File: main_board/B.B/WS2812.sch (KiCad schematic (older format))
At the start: 120 parts

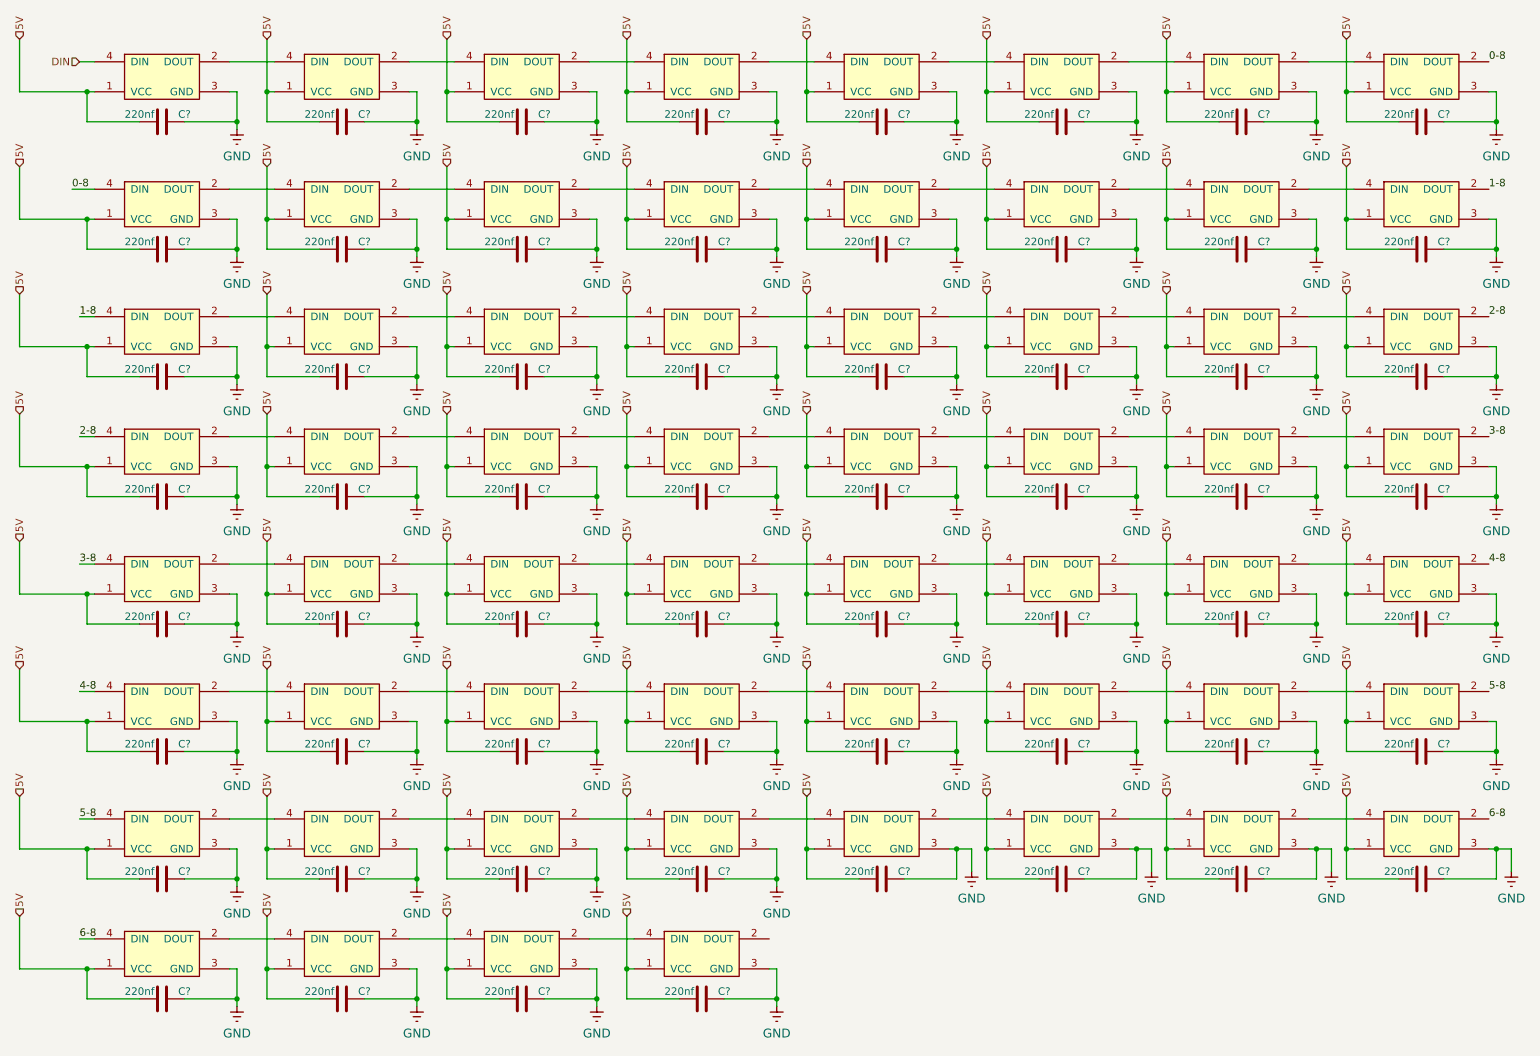
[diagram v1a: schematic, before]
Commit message: complete_preparation_to_drawing_PCB
footprint for all component and LCSC code for everything for mounting in JLCPCB
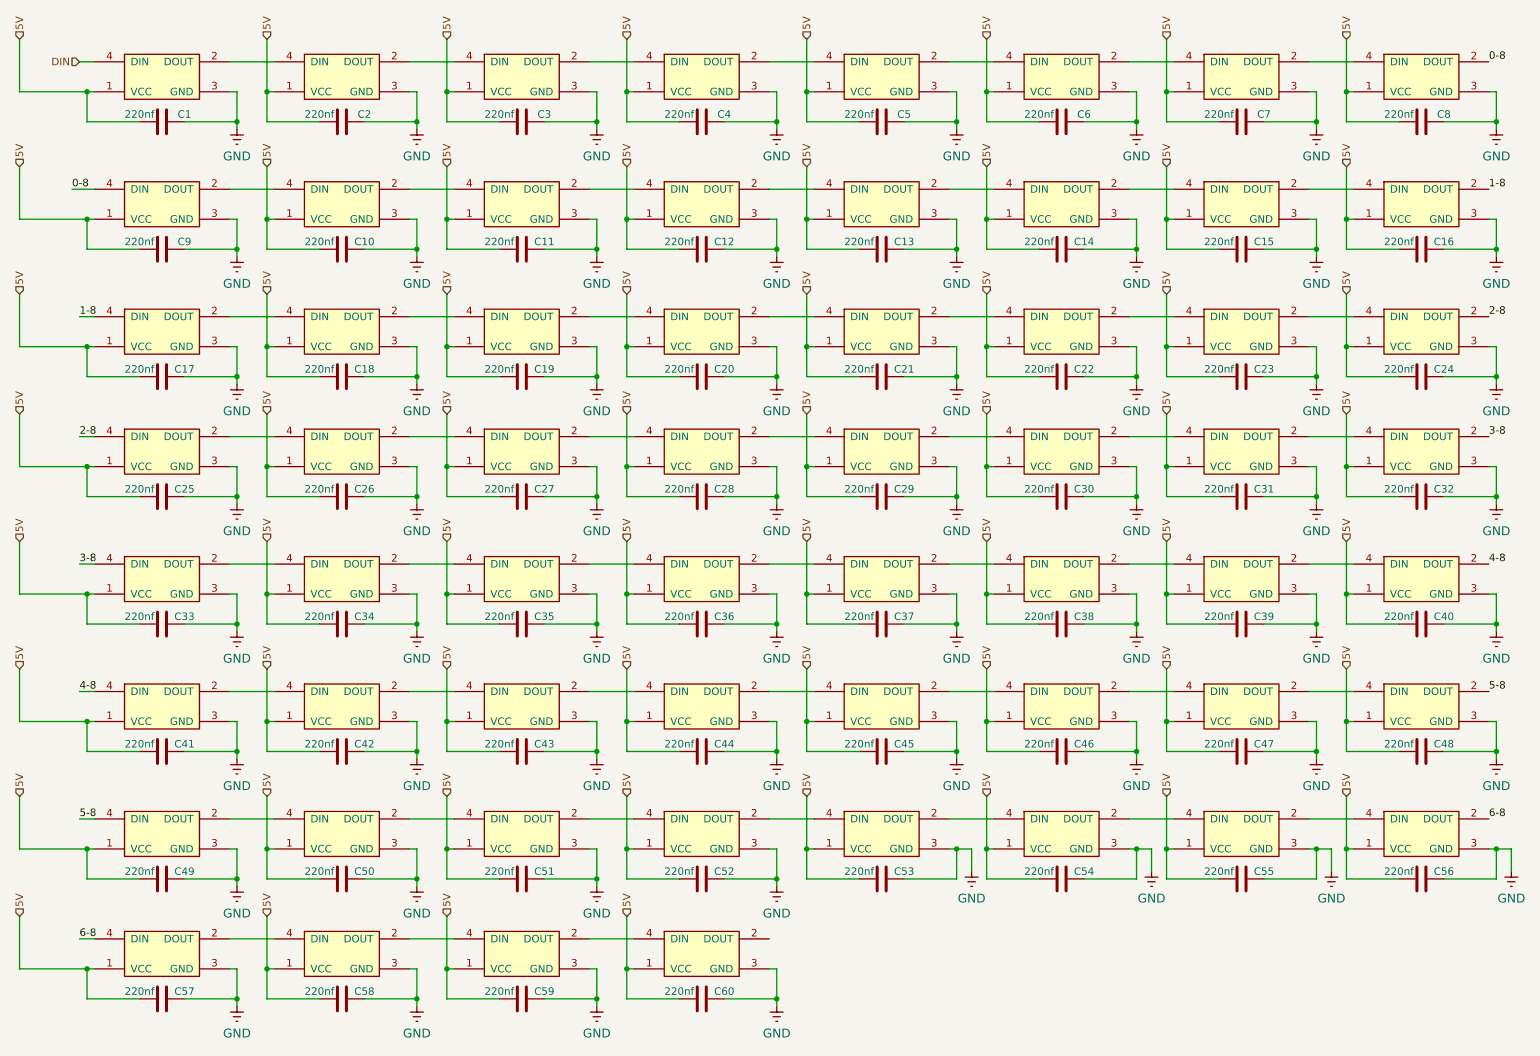
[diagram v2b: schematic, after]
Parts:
- removed U? (x59): WS2812, symbol B.B-eagle-import:WS2812
- added U10, U11, U12, U13, U14, U15, U16, U17, U18, U19, U2, U20, U21, U22, U23, U24, U25, U26, U27, U28, U29, U3, U30, U31, U32, U33, U34, U35, U36, U37, U38, U39, U4, U40, U41, U42, U43, U44, U45, U46, U47, U48, U49, U5, U50, U51, U52, U53, U54, U55, U56, U57, U58, U59, U6, U7, U74, U8, U9: WS2812, BB:WS2812, symbol B.B-eagle-import:WS2812
- U1: renamed from ?; footprint (none) -> BB:WS2812
- gave numbers to parts that had none: 60
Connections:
- net 0-8: now also U8.2 (DOUT), U9.4 (DIN)
- net 1-8: now also U16.2 (DOUT), U17.4 (DIN)
- net 2-8: now also U24.2 (DOUT), U25.4 (DIN)
- net 3-8: now also U32.2 (DOUT), U33.4 (DIN)
- net 4-8: now also U40.2 (DOUT), U41.4 (DIN)
- net 5-8: now also U48.2 (DOUT), U49.4 (DIN)
- net 5V: now also U10.1 (VCC), U11.1 (VCC), U12.1 (VCC), U13.1 (VCC), U14.1 (VCC), U15.1 (VCC), U16.1 (VCC), U17.1 (VCC), U18.1 (VCC), U19.1 (VCC), U2.1 (VCC), U20.1 (VCC), U21.1 (VCC), U22.1 (VCC), U23.1 (VCC), U24.1 (VCC), U25.1 (VCC), U26.1 (VCC), U27.1 (VCC), U28.1 (VCC), U29.1 (VCC), U3.1 (VCC), U30.1 (VCC), U31.1 (VCC), U32.1 (VCC), U33.1 (VCC), U34.1 (VCC), U35.1 (VCC), U36.1 (VCC), U37.1 (VCC), U38.1 (VCC), U39.1 (VCC), U4.1 (VCC), U40.1 (VCC), U41.1 (VCC), U42.1 (VCC), U43.1 (VCC), U44.1 (VCC), U45.1 (VCC), U46.1 (VCC), U47.1 (VCC), U48.1 (VCC), U49.1 (VCC), U5.1 (VCC), U50.1 (VCC), U51.1 (VCC), U52.1 (VCC), U53.1 (VCC), U54.1 (VCC), U55.1 (VCC), U56.1 (VCC), U57.1 (VCC), U58.1 (VCC), U59.1 (VCC), U6.1 (VCC), U7.1 (VCC), U74.1 (VCC), U8.1 (VCC), U9.1 (VCC)
- net 6-8: now also U56.2 (DOUT), U57.4 (DIN)
- net at U1.2 (DOUT): now also U2.4 (DIN)
- net at C2.1: now also U2.3 (GND)
- net at C3.1: now also U3.3 (GND)
- net at C4.1: now also U4.3 (GND)
- net at C5.1: now also U5.3 (GND)
- net at C6.1: now also U6.3 (GND)
- net at C7.1: now also U7.3 (GND)
- net at C8.1: now also U8.3 (GND)
- net at C9.1: now also U9.3 (GND)
- net at C10.1: now also U10.3 (GND)
- net at C11.1: now also U11.3 (GND)
- net at C12.1: now also U12.3 (GND)
- net at C13.1: now also U13.3 (GND)
- net at C14.1: now also U14.3 (GND)
- net at C15.1: now also U15.3 (GND)
- net at C16.1: now also U16.3 (GND)
- net at C17.1: now also U17.3 (GND)
- net at C18.1: now also U18.3 (GND)
- net at C19.1: now also U19.3 (GND)
- net at C20.1: now also U20.3 (GND)
- net at C21.1: now also U21.3 (GND)
- net at C22.1: now also U22.3 (GND)
- net at C23.1: now also U23.3 (GND)
- net at C24.1: now also U24.3 (GND)
- net at C25.1: now also U25.3 (GND)
- net at C26.1: now also U26.3 (GND)
- net at C27.1: now also U27.3 (GND)
- net at C28.1: now also U28.3 (GND)
- net at C29.1: now also U29.3 (GND)
- net at C30.1: now also U30.3 (GND)
- net at C31.1: now also U31.3 (GND)
- net at C32.1: now also U32.3 (GND)
- net at C33.1: now also U33.3 (GND)
- net at C34.1: now also U34.3 (GND)
- net at C35.1: now also U35.3 (GND)
- net at C36.1: now also U36.3 (GND)
- net at C37.1: now also U37.3 (GND)
- net at C38.1: now also U38.3 (GND)
- net at C39.1: now also U39.3 (GND)
- net at C40.1: now also U40.3 (GND)
- net at C48.1: now also U48.3 (GND)
- net at C47.1: now also U47.3 (GND)
- net at C46.1: now also U46.3 (GND)
- net at C45.1: now also U45.3 (GND)
- net at C44.1: now also U44.3 (GND)
- net at C43.1: now also U43.3 (GND)
- net at C42.1: now also U42.3 (GND)
- net at C41.1: now also U41.3 (GND)
- net at C49.1: now also U49.3 (GND)
- net at C50.1: now also U50.3 (GND)
- net at C51.1: now also U51.3 (GND)
- net at C52.1: now also U52.3 (GND)
- net at C53.1: now also U53.3 (GND)
- net at C54.1: now also U54.3 (GND)
- net at C55.1: now also U55.3 (GND)
- net at C56.1: now also U56.3 (GND)
- net at C57.1: now also U57.3 (GND)
- net at C58.1: now also U58.3 (GND)
- net at C59.1: now also U59.3 (GND)
- net at C60.1: now also U74.3 (GND)
- new net: U2.2 (DOUT), U3.4 (DIN)
- new net: U3.2 (DOUT), U4.4 (DIN)
- new net: U4.2 (DOUT), U5.4 (DIN)
- new net: U5.2 (DOUT), U6.4 (DIN)
- new net: U6.2 (DOUT), U7.4 (DIN)
- new net: U7.2 (DOUT), U8.4 (DIN)
- new net: U10.4 (DIN), U9.2 (DOUT)
- new net: U10.2 (DOUT), U11.4 (DIN)
- new net: U11.2 (DOUT), U12.4 (DIN)
- new net: U12.2 (DOUT), U13.4 (DIN)
- new net: U13.2 (DOUT), U14.4 (DIN)
- new net: U14.2 (DOUT), U15.4 (DIN)
- new net: U15.2 (DOUT), U16.4 (DIN)
- new net: U17.2 (DOUT), U18.4 (DIN)
- new net: U18.2 (DOUT), U19.4 (DIN)
- new net: U19.2 (DOUT), U20.4 (DIN)
- new net: U20.2 (DOUT), U21.4 (DIN)
- new net: U21.2 (DOUT), U22.4 (DIN)
- new net: U22.2 (DOUT), U23.4 (DIN)
- new net: U23.2 (DOUT), U24.4 (DIN)
- new net: U25.2 (DOUT), U26.4 (DIN)
- new net: U26.2 (DOUT), U27.4 (DIN)
- new net: U27.2 (DOUT), U28.4 (DIN)
- new net: U28.2 (DOUT), U29.4 (DIN)
- new net: U29.2 (DOUT), U30.4 (DIN)
- new net: U30.2 (DOUT), U31.4 (DIN)
- new net: U31.2 (DOUT), U32.4 (DIN)
- new net: U33.2 (DOUT), U34.4 (DIN)
- new net: U34.2 (DOUT), U35.4 (DIN)
- new net: U35.2 (DOUT), U36.4 (DIN)
- new net: U36.2 (DOUT), U37.4 (DIN)
- new net: U37.2 (DOUT), U38.4 (DIN)
- new net: U38.2 (DOUT), U39.4 (DIN)
- new net: U39.2 (DOUT), U40.4 (DIN)
- new net: U41.2 (DOUT), U42.4 (DIN)
- new net: U42.2 (DOUT), U43.4 (DIN)
- new net: U43.2 (DOUT), U44.4 (DIN)
- new net: U44.2 (DOUT), U45.4 (DIN)
- new net: U45.2 (DOUT), U46.4 (DIN)
- new net: U46.2 (DOUT), U47.4 (DIN)
- new net: U47.2 (DOUT), U48.4 (DIN)
- new net: U49.2 (DOUT), U50.4 (DIN)
- new net: U50.2 (DOUT), U51.4 (DIN)
- new net: U51.2 (DOUT), U52.4 (DIN)
- new net: U52.2 (DOUT), U53.4 (DIN)
- new net: U53.2 (DOUT), U54.4 (DIN)
- new net: U54.2 (DOUT), U55.4 (DIN)
- new net: U55.2 (DOUT), U56.4 (DIN)
- new net: U57.2 (DOUT), U58.4 (DIN)
- new net: U58.2 (DOUT), U59.4 (DIN)
- new net: U59.2 (DOUT), U74.4 (DIN)

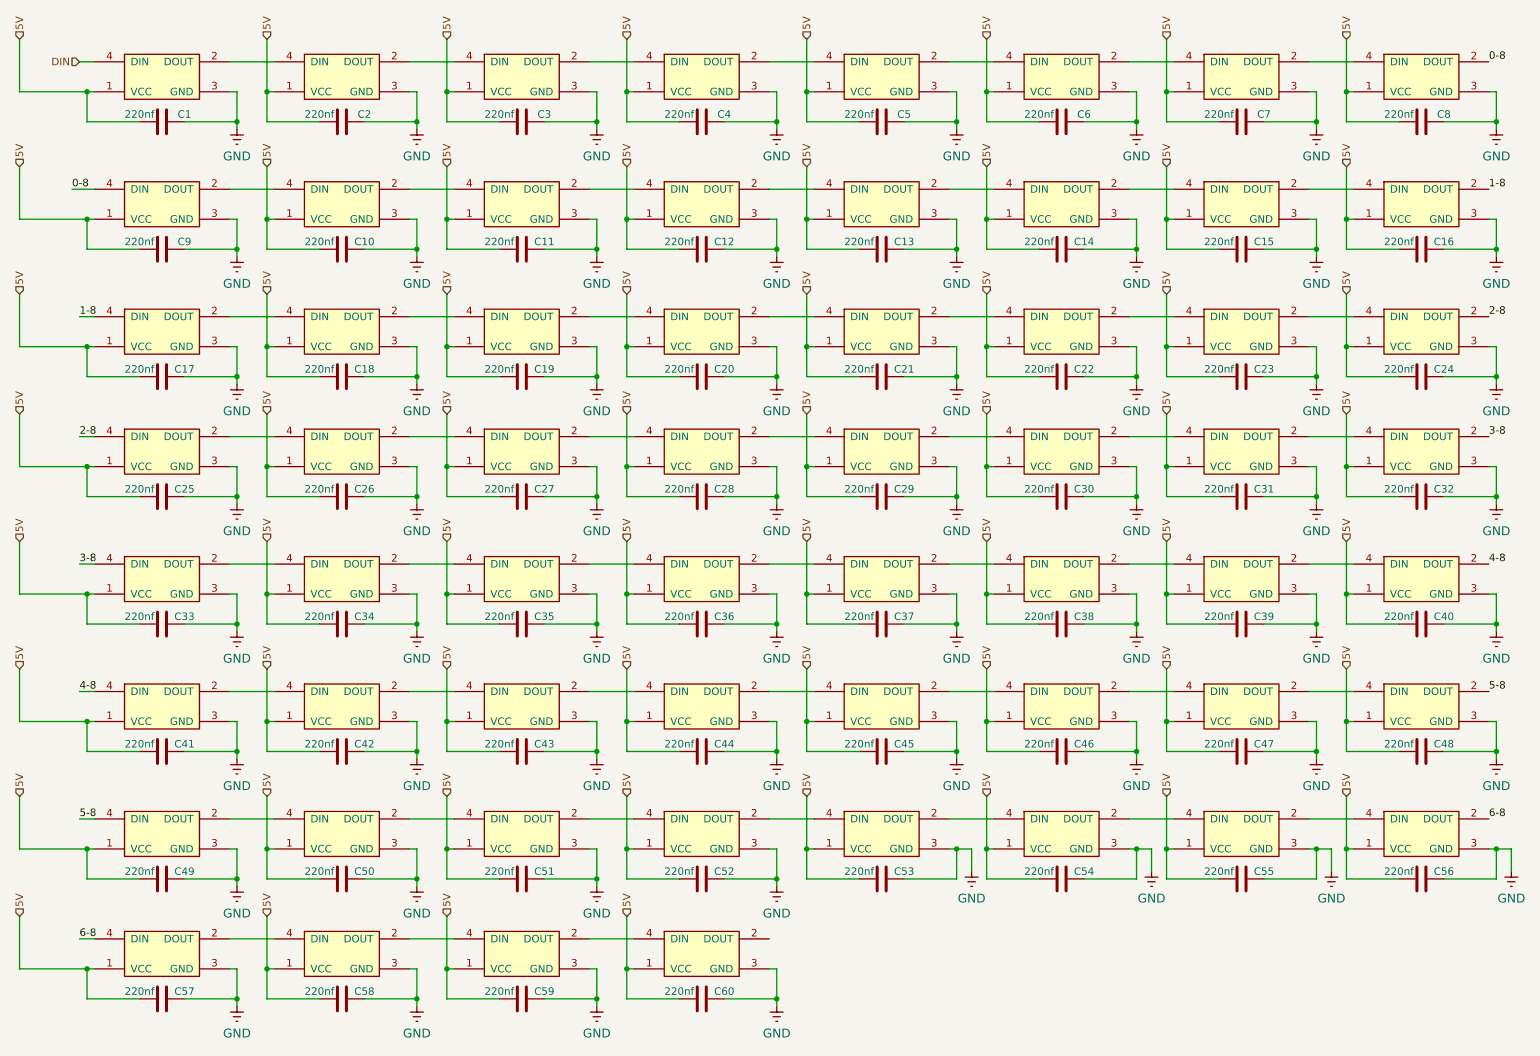
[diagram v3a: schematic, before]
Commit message: orezavani
smazaní A9G, SD karty, a zvuku
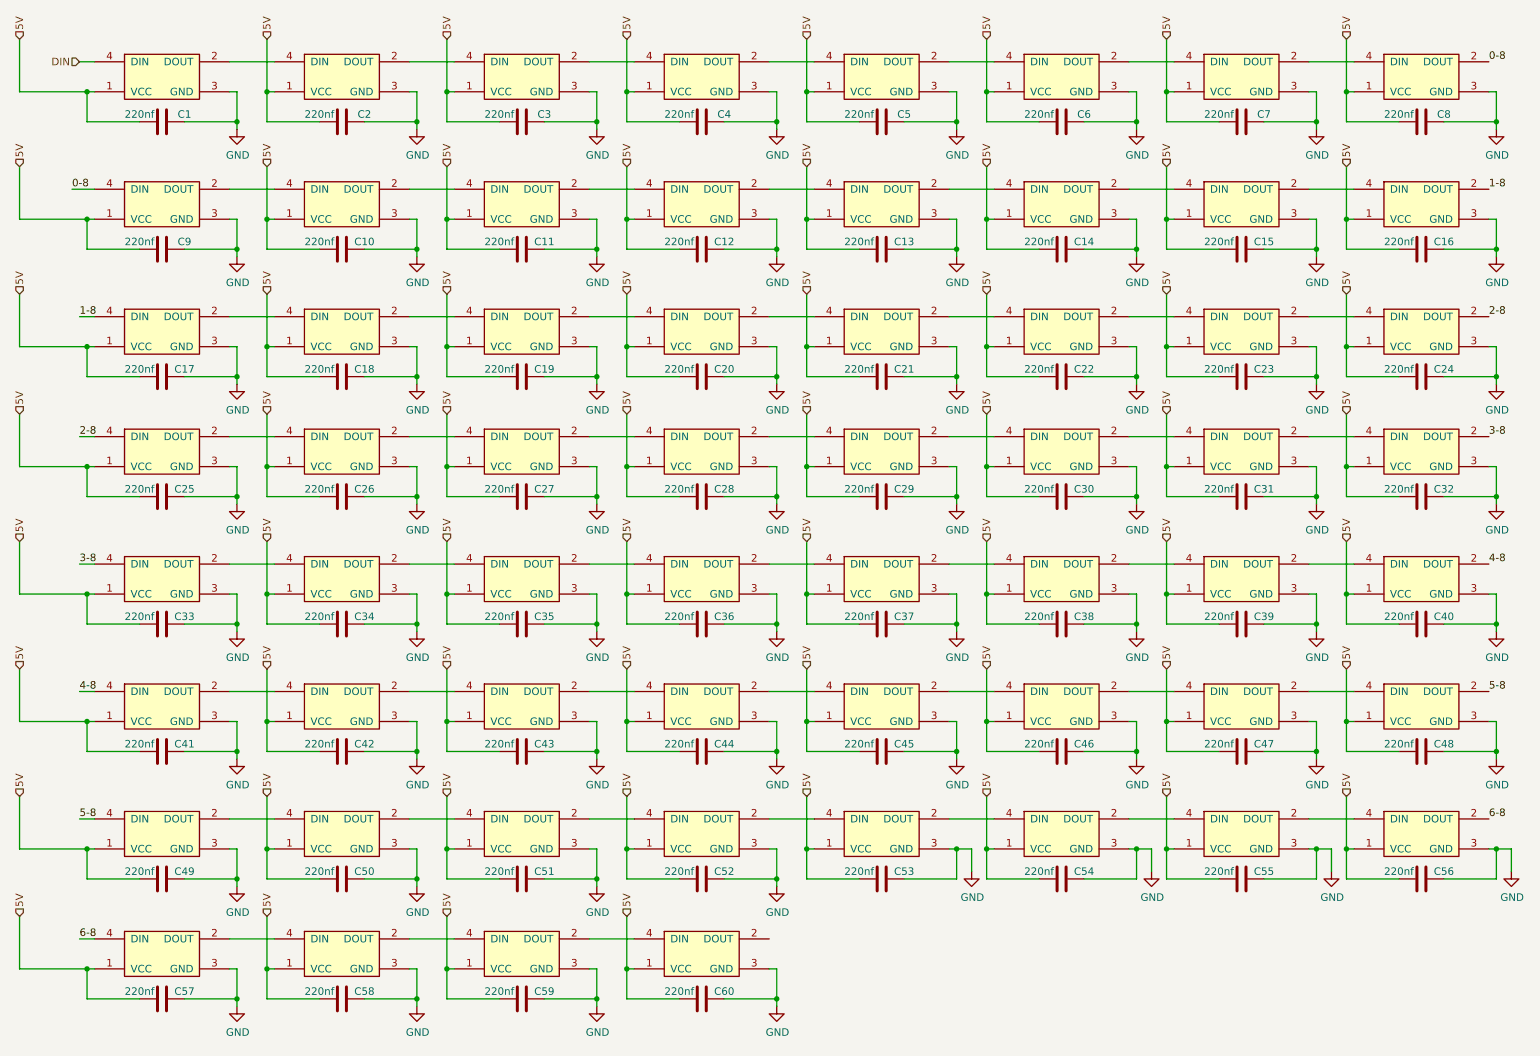
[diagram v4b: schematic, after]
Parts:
- removed U1, U10, U11, U12, U13, U14, U15, U16, U17, U18, U19, U2, U20, U21, U22, U23, U24, U25, U26, U27, U28, U29, U3, U30, U31, U32, U33, U34, U35, U36, U37, U38, U39, U4, U40, U41, U42, U43, U44, U45, U46, U47, U48, U49, U5, U50, U51, U52, U53, U54, U55, U56, U57, U58, U59, U6, U7, U74, U8, U9: WS2812, BB:WS2812, symbol B.B-eagle-import:WS2812
- added U? (x60): WS2812, BB:WS2812, symbol B.B-eagle-import:WS2812
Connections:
- net 0-8: now also U?.2 (DOUT), U?.4 (DIN)
- net 1-8: now also U?.2 (DOUT), U?.4 (DIN)
- net 2-8: now also U?.2 (DOUT), U?.4 (DIN)
- net 3-8: now also U?.2 (DOUT), U?.4 (DIN)
- net 4-8: now also U?.2 (DOUT), U?.4 (DIN)
- net 5-8: now also U?.2 (DOUT), U?.4 (DIN)
- net 5V: now also U?.1 (VCC), U?.1 (VCC), U?.1 (VCC), U?.1 (VCC), U?.1 (VCC), U?.1 (VCC), U?.1 (VCC), U?.1 (VCC), U?.1 (VCC), U?.1 (VCC), U?.1 (VCC), U?.1 (VCC), U?.1 (VCC), U?.1 (VCC), U?.1 (VCC), U?.1 (VCC), U?.1 (VCC), U?.1 (VCC), U?.1 (VCC), U?.1 (VCC), U?.1 (VCC), U?.1 (VCC), U?.1 (VCC), U?.1 (VCC), U?.1 (VCC), U?.1 (VCC), U?.1 (VCC), U?.1 (VCC), U?.1 (VCC), U?.1 (VCC), U?.1 (VCC), U?.1 (VCC), U?.1 (VCC), U?.1 (VCC), U?.1 (VCC), U?.1 (VCC), U?.1 (VCC), U?.1 (VCC), U?.1 (VCC), U?.1 (VCC), U?.1 (VCC), U?.1 (VCC), U?.1 (VCC), U?.1 (VCC), U?.1 (VCC), U?.1 (VCC), U?.1 (VCC), U?.1 (VCC), U?.1 (VCC), U?.1 (VCC), U?.1 (VCC), U?.1 (VCC), U?.1 (VCC), U?.1 (VCC), U?.1 (VCC), U?.1 (VCC), U?.1 (VCC), U?.1 (VCC), U?.1 (VCC), U?.1 (VCC)
- net 6-8: now also U?.2 (DOUT), U?.4 (DIN)
- net DIN: now also U?.4 (DIN)
- net GND: now reaches C1.1
- net GND: now also C10.1, C11.1, C12.1, C13.1, C14.1, C15.1, C16.1, C17.1, C18.1, C19.1, C2.1, C20.1, C21.1, C22.1, C23.1, C24.1, C25.1, C26.1, C27.1, C28.1, C29.1, C3.1, C30.1, C31.1, C32.1, C33.1, C34.1, C35.1, C36.1, C37.1, C38.1, C39.1, C4.1, C40.1, C41.1, C42.1, C43.1, C44.1, C45.1, C46.1, C47.1, C48.1, C49.1, C5.1, C50.1, C51.1, C52.1, C53.1, C54.1, C55.1, C56.1, C57.1, C58.1, C59.1, C6.1, C60.1, C7.1, C8.1, C9.1, U?.3 (GND), U?.3 (GND), U?.3 (GND), U?.3 (GND), U?.3 (GND), U?.3 (GND), U?.3 (GND), U?.3 (GND), U?.3 (GND), U?.3 (GND), U?.3 (GND), U?.3 (GND), U?.3 (GND), U?.3 (GND), U?.3 (GND), U?.3 (GND), U?.3 (GND), U?.3 (GND), U?.3 (GND), U?.3 (GND), U?.3 (GND), U?.3 (GND), U?.3 (GND), U?.3 (GND), U?.3 (GND), U?.3 (GND), U?.3 (GND), U?.3 (GND), U?.3 (GND), U?.3 (GND), U?.3 (GND), U?.3 (GND), U?.3 (GND), U?.3 (GND), U?.3 (GND), U?.3 (GND), U?.3 (GND), U?.3 (GND), U?.3 (GND), U?.3 (GND), U?.3 (GND), U?.3 (GND), U?.3 (GND), U?.3 (GND), U?.3 (GND), U?.3 (GND), U?.3 (GND), U?.3 (GND), U?.3 (GND), U?.3 (GND), U?.3 (GND), U?.3 (GND), U?.3 (GND), U?.3 (GND), U?.3 (GND), U?.3 (GND), U?.3 (GND), U?.3 (GND), U?.3 (GND), U?.3 (GND)
- new net: U?.2 (DOUT), U?.4 (DIN) (x52)

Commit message: nabijecka
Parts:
- gave numbers to parts that had none: 60
